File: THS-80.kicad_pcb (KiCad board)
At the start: 4 copper layers, 101.6 x 102.1 mm, 117 parts, among them J1 USB_B_Micro, J10 CT0, J2 RC80 Bus, J3 RC80 Expansion, J4 IDE, J5 JTAG, J6 PMOD, J7 PIO Header, J8 Port A, J9 Port A, SW1 Reset, SW2 SW_DIP_x06, SW3 User PB, U1 MAX40203AUK, U10 AP7381-33SA, U11 TXS0108EPW, U12 74HCT3G04, U2 DS1813R-5+T&R, U3 EPM7064STC100, U4 Z84C0010AEG, U5 IS62C5128BL-45TLI, U6 SST39SF040, U7 Z84C2010AEG, U8 Z84C4310AEG, U9 Z84C3010AEG, X1 CFPS-72 50mhz

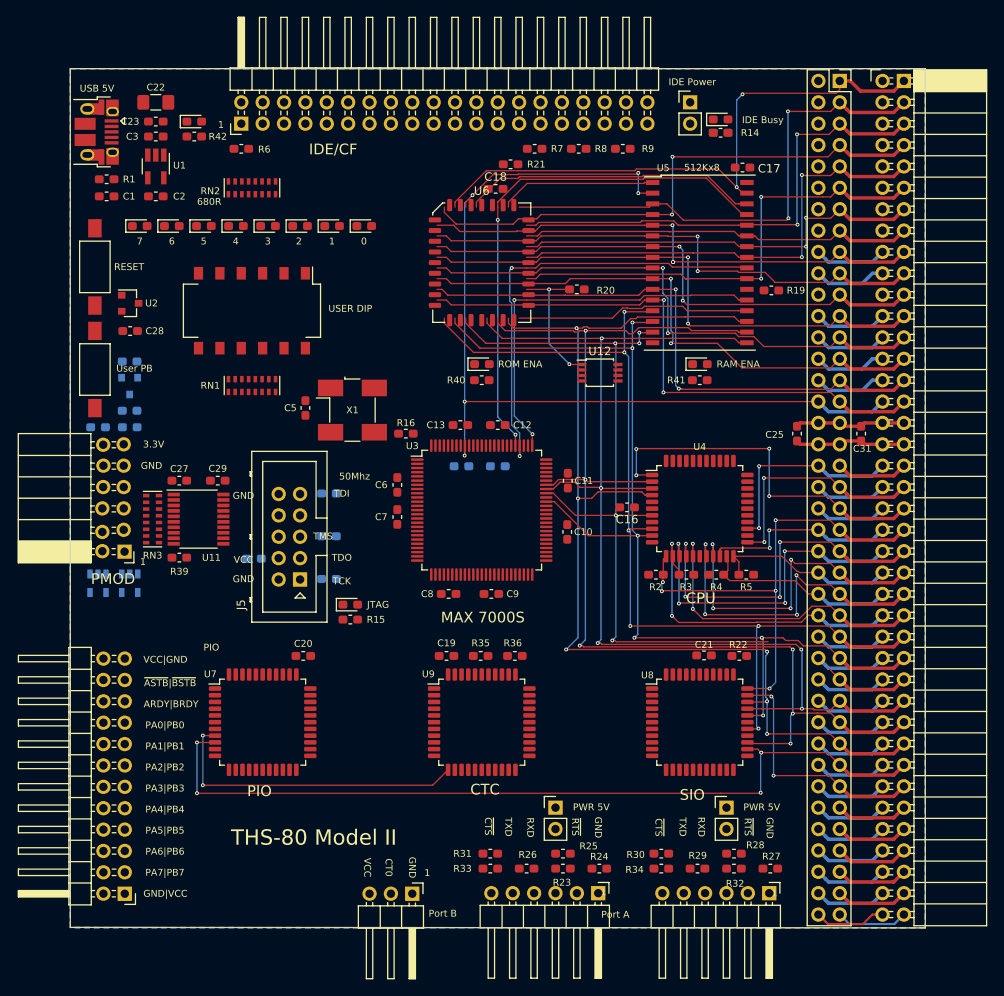
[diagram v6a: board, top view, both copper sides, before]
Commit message: layout changes, silkscreen fixes
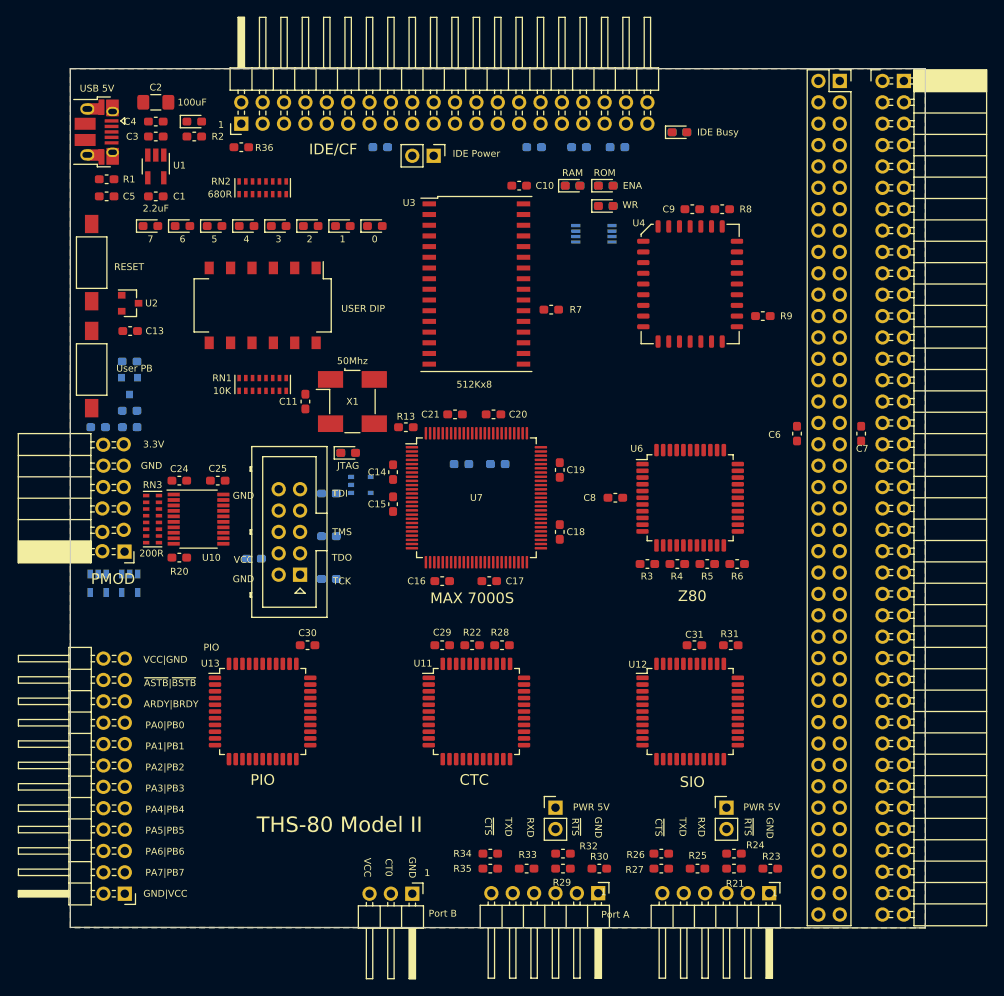
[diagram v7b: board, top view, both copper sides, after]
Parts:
- removed the D13 at (150.5, 66.7)
- removed the D14 at (176.4, 66.7)
- removed the R40 at (150.5, 68.6)
- removed R41: 360R, Resistor_SMD:R_0603_1608Metric_Pad1.05x0.95mm_HandSolder
- removed the U12 at (164.5, 67.7)
- removed the U6 at (150.5, 54.6)
- added D2: GRN, LED_SMD:LED_0603_1608Metric_Pad1.05x0.95mm_HandSolder, F.Cu at (165.2, 45.5)
- added D3: GRN, LED_SMD:LED_0603_1608Metric_Pad1.05x0.95mm_HandSolder, F.Cu at (161.3, 45.5)
- added D4: RED, LED_SMD:LED_0603_1608Metric_Pad1.05x0.95mm_HandSolder, F.Cu at (165.2, 47.9)
- added R10: 1K, Resistor_SMD:R_0603_1608Metric_Pad1.05x0.95mm_HandSolder, B.Cu at (165.2, 45.5)
- added R11: 1K, Resistor_SMD:R_0603_1608Metric_Pad1.05x0.95mm_HandSolder, B.Cu at (161.3, 45.5)
- added R12: 360R, Resistor_SMD:R_0603_1608Metric_Pad1.05x0.95mm_HandSolder, B.Cu at (165.2, 47.9)
- added U3: IS62C5128BL-45TLI, Package_SO:TSOP-II-32_21.0x10.2mm_P1.27mm, F.Cu at (149.9, 57.1)
- added U4: SST39SF040, Package_LCC:PLCC-32_11.4x14.0mm_P1.27mm, F.Cu at (175.3, 57.1)
- added U8: 74LVC1G04, Package_SO:TSOP-5_1.65x3.05mm_P0.95mm, B.Cu at (136.1, 81.0)
- R19: renamed from R15; moved to B.Cu
- R37: renamed from R7; moved to B.Cu
- R38: renamed from R8; moved to B.Cu
- R39: renamed from R9; moved to B.Cu
- R40: renamed from R14; moved to B.Cu
- U5: value IS62C5128BL-45TLI -> 74LVC2G02; footprint Package_SO:TSOP-II-32_21.0x10.2mm_P1.27mm -> Package_SO:TSSOP-8_3x3mm_P0.65mm; moved to B.Cu
- moved C28 40.5 mm to (138.4, 40.9), turned to 180 degrees
- moved JP3 31.1 mm to (144.8, 41.9), turned to 270 degrees
- moved R7 26.3 mm to (158.8, 60.2)
- moved R8 25.7 mm to (179.1, 48.3)
- moved R9 22.3 mm to (183.9, 61.0)
- moved R19 19.8 mm to (134.6, 77.2)
- moved D13 18.0 mm to (134.6, 77.2)
- moved U5 13.0 mm to (163.8, 51.2), turned to 180 degrees
- moved C9 7.76 mm to (175.5, 48.3)
- moved D16 5.12 mm to (174.0, 39.1)
- moved R40 4.89 mm to (174.0, 39.1)
- moved C10 2.82 mm to (154.9, 45.5), turned to 180 degrees
- moved R28 1.98 mm to (152.9, 100.1)
- moved C8 1.81 mm to (166.4, 82.5)
- moved U6 1.72 mm to (175.3, 82.5)
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- renumbered C2 to C1, C18 to C10, C5 to C11, C30 to C12, C28 to C13, C6 to C14, C7 to C15, C8 to C16, C9 to C17, C10 to C18, C11 to C19, C22 to C2, C12 to C20, C13 to C21, C14 to C22, C15 to C23, C27 to C24, C29 to C25, C24 to C26, C26 to C27, C4 to C28, C19 to C29, C20 to C30, C21 to C31, C23 to C4, C1 to C5, C25 to C6, C31 to C7, C16 to C8, C17 to C9, D15 to D1, D9 to D10, D10 to D11, D11 to D12, D2 to D13, D3 to D14, D12 to D15, D1 to D16, D4 to D5, D5 to D6, D6 to D7, D7 to D8, D8 to D9, J7 to J10, J5 to J4, J6 to J5, J10 to J6, J9 to J7, J4 to J9, JP3 to JP1, JP1 to JP3, R16 to R13, R17 to R14, R18 to R15, R11 to R16, R12 to R17, R10 to R18, R42 to R2, R39 to R20, R32 to R21, R35 to R22, R27 to R23, R28 to R24, R29 to R25, R30 to R26, R34 to R27, R36 to R28, R23 to R29, R2 to R3, R24 to R30, R22 to R31, R25 to R32, R26 to R33, R31 to R34, R33 to R35, R6 to R36, R3 to R4, R4 to R5, R5 to R6, R19 to R7, R21 to R8, R20 to R9, U11 to U10, U9 to U11, U8 to U12, U7 to U13, U4 to U6, U3 to U7, U10 to U9
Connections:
- C1 pad 1: +5V -> VCC
- C10 pad 1: +5V -> VCC
- C11 pad 1: +5V -> VCC
- C12 pad 1: +5V -> VCC
- C14 pad 1: +5V -> VCC
- C15 pad 1: +5V -> VCC
- C16 pad 1: +5V -> VCC
- C17 pad 1: +5V -> VCC
- C18 pad 1: +5V -> VCC
- C19 pad 1: +5V -> VCC
- C20 pad 1: +5V -> VCC
- C21 pad 1: +5V -> VCC
- C22 pad 1: +5V -> VCC
- C25 pad 1: +5V -> VCC
- C28 pad 1: +5V -> VCC
- C29 pad 1: +5V -> VCC
- C30 pad 1: +5V -> VCC
- C31 pad 1: +5V -> VCC
- C6 pad 1: +5V -> VCC
- C7 pad 1: +5V -> VCC
- C8 pad 1: +5V -> VCC
- C9 pad 1: +5V -> VCC
- D1 pad 2: +5V -> VCC
- J10 pad 1: +5V -> VCC
- J10 pad 24: +5V -> VCC
- J2 pad 35: +5V -> VCC
- J2 pad 36: +5V -> VCC
- J3 pad 35: +5V -> VCC
- J3 pad 36: +5V -> VCC
- J4 pad 4: +5V -> VCC
- J6 pad 3: +5V -> VCC
- JP1 pad 1: +5V -> VCC
- JP2 pad 1: +5V -> VCC
- JP3 pad 2: +5V -> VCC
- R14 pad 2: +5V -> VCC
- R15 pad 2: +5V -> VCC
- R16 pad 1: +5V -> VCC
- R17 pad 1: +5V -> VCC
- R21 pad 1: +5V -> VCC
- R22 pad 1: +5V -> VCC
- R28 pad 1: +5V -> VCC
- R29 pad 1: +5V -> VCC
- R3 pad 1: +5V -> VCC
- R31 pad 1: +5V -> VCC
- R36 pad 1: +5V -> VCC
- R37 pad 1: +5V -> VCC
- R38 pad 1: +5V -> VCC
- R39 pad 1: +5V -> VCC
- R4 pad 1: +5V -> VCC
- R40 pad 1: +5V -> VCC
- R5 pad 1: +5V -> VCC
- R6 pad 1: +5V -> VCC
- R7 pad 1: +5V -> VCC
- R8 pad 1: +5V -> VCC
- R9 pad 1: +5V -> VCC
- RN1 pad 10: +5V -> VCC
- RN1 pad 11: +5V -> VCC
- RN1 pad 12: +5V -> VCC
- RN1 pad 13: +5V -> VCC
- RN1 pad 14: +5V -> VCC
- RN1 pad 15: +5V -> VCC
- RN1 pad 16: +5V -> VCC
- RN1 pad 9: +5V -> VCC
- RN2 pad 10: +5V -> VCC
- RN2 pad 11: +5V -> VCC
- RN2 pad 12: +5V -> VCC
- RN2 pad 13: +5V -> VCC
- RN2 pad 14: +5V -> VCC
- RN2 pad 15: +5V -> VCC
- RN2 pad 16: +5V -> VCC
- RN2 pad 9: +5V -> VCC
- U1 pad 5: +5V -> VCC
- U10 pad 19: +5V -> VCC
- U11 pad 43: +5V -> VCC
- U12 pad 37: +5V -> VCC
- U13 pad 34: +5V -> VCC
- U2 pad 2: +5V -> VCC
- U5 pad 1: /A17 -> /RAM_~CE
- U5 pad 2: /A16 -> /RAM_~CE
- U5 pad 3: /A14 -> Net-(D4-Pad2)
- U5 pad 4: /A12 -> GND
- U5 pad 5: /A7 -> /ROM_~CE
- U5 pad 6: /A6 -> /~WR
- U5 pad 7: /A5 -> Net-(D2-Pad1)
- U5 pad 8: /A4 -> VCC
- U6 pad 6: +5V -> VCC
- U7 pad 18: +5V -> VCC
- U7 pad 3: +5V -> VCC
- U7 pad 34: +5V -> VCC
- U7 pad 39: +5V -> VCC
- U7 pad 51: +5V -> VCC
- U7 pad 66: +5V -> VCC
- U7 pad 82: +5V -> VCC
- U7 pad 91: +5V -> VCC
- U9 pad 1: +5V -> VCC
- X1 pad 1: +5V -> VCC
- X1 pad 4: +5V -> VCC
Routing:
- net /D4: track 138.7 -> 0.00 mm, vias 6 -> 0
- net /D3: track 134.3 -> 0.00 mm, vias 5 -> 0
- net /D5: track 132.7 -> 0.00 mm, vias 6 -> 0
- net /D6: track 128.3 -> 0.00 mm, vias 4 -> 0
- net /D1: track 122.7 -> 0.00 mm, vias 6 -> 0
- net /D0: track 115.1 -> 0.00 mm, vias 6 -> 0
- net /D7: track 113.0 -> 0.00 mm, vias 6 -> 0
- net /A16: track 109.9 -> 0.00 mm, vias 5 -> 0
- net /D2: track 103.3 -> 0.00 mm, vias 5 -> 0
- net /~WR: track 101.6 -> 0.00 mm, vias 6 -> 0
- net /~RD: track 92.7 -> 0.00 mm, vias 6 -> 0
- net /A15: track 70.9 -> 0.00 mm, vias 2 -> 0
- net /A1: track 69.1 -> 0.00 mm, vias 2 -> 0
- net /A0: track 68.5 -> 0.00 mm, vias 2 -> 0
- net /A2: track 66.5 -> 0.00 mm, vias 2 -> 0
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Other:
- board text added: "ENA"
- board text added: "RAM"
- board text added: "ROM"
- board text added: "WR"
- board text added: "Z80"
- board text removed: "CPU"
- board text removed: "RAM ENA"
- board text removed: "ROM ENA"

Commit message: more layout changes
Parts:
- moved D2 5.98 mm to (164.0, 51.3)
- moved R10 5.98 mm to (164.0, 51.3)
- moved D3 5.98 mm to (160.0, 51.3)
- moved R11 5.98 mm to (160.0, 51.3)
- moved D4 5.48 mm to (164.0, 53.2)
- moved R12 5.48 mm to (164.0, 53.2)
- moved U5 5.48 mm to (162.6, 56.5)
- moved C10 0.25 mm to (154.9, 45.2)
- moved C9 0.25 mm to (175.5, 48.0)
- moved R8 0.25 mm to (179.1, 48.0)
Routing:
- net /A15: track 0.00 -> 0.95 mm
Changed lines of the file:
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@@
     (thickness 1.6)
     (drawings 76)
-    (tracks 0)
+    (tracks 1)
     (zones 0)
     (modules 120)
@@
     (1 In1.Cu signal hide)
     (2 In2.Cu power hide)
-    (31 B.Cu signal)
+    (31 B.Cu signal hide)
     (34 B.Paste user hide)
     (35 F.Paste user hide)
@@
     (add_net "Net-(D8-Pad2)")
     (add_net "Net-(D9-Pad2)")
-    (add_net "Net-(J1-Pad2)")
-    (add_net "Net-(J1-Pad3)")
-    (add_net "Net-(J2-Pad10)")
-    (add_net "Net-(J2-Pad12)")
-    (add_net "Net-(J2-Pad14)")
-    (add_net "Net-(J2-Pad16)")
-    (add_net "Net-(J2-Pad2)")
-    (add_net "Net-(J2-Pad4)")
-    (add_net "Net-(J2-Pad6)")
-    (add_net "Net-(J2-Pad8)")
-    (add_net "Net-(J3-Pad10)")
-    (add_net "Net-(J3-Pad12)")
-    (add_net "Net-(J3-Pad14)")
-    (add_net "Net-(J3-Pad16)")
-    (add_net "Net-(J3-Pad2)")
-    (add_net "Net-(J3-Pad4)")
-    (add_net "Net-(J3-Pad6)")
-    (add_net "Net-(J3-Pad8)")
-    (add_net "Net-(J4-Pad6)")
-    (add_net "Net-(J4-Pad7)")
-    (add_net "Net-(J4-Pad8)")
     (add_net "Net-(J7-Pad3)")
     (add_net "Net-(J8-Pad3)")
-    (add_net "Net-(J9-Pad10)")
-    (add_net "Net-(J9-Pad12)")
-    (add_net "Net-(J9-Pad14)")
-    (add_net "Net-(J9-Pad16)")
-    (add_net "Net-(J9-Pad18)")
     (add_net "Net-(J9-Pad20)")
-    (add_net "Net-(J9-Pad21)")
-    (add_net "Net-(J9-Pad27)")
-    (add_net "Net-(J9-Pad28)")
     (add_net "Net-(J9-Pad29)")
-    (add_net "Net-(J9-Pad31)")
-    (add_net "Net-(J9-Pad32)")
     (add_net "Net-(J9-Pad34)")
     (add_net "Net-(J9-Pad38)")
-    (add_net "Net-(J9-Pad4)")
-    (add_net "Net-(J9-Pad6)")
-    (add_net "Net-(J9-Pad8)")
     (add_net "Net-(R13-Pad1)")
     (add_net "Net-(R14-Pad1)")
-    (add_net "Net-(RN1-Pad4)")
-    (add_net "Net-(RN1-Pad5)")
     (add_net "Net-(RN3-Pad10)")
     (add_net "Net-(RN3-Pad11)")
@@
     (add_net "Net-(RN3-Pad16)")
     (add_net "Net-(RN3-Pad9)")
-    (add_net "Net-(U1-Pad4)")
-    (add_net "Net-(U11-Pad11)")
-    (add_net "Net-(U11-Pad15)")
-    (add_net "Net-(U11-Pad16)")
-    (add_net "Net-(U11-Pad17)")
-    (add_net "Net-(U11-Pad19)")
-    (add_net "Net-(U11-Pad20)")
-    (add_net "Net-(U11-Pad24)")
-    (add_net "Net-(U11-Pad26)")
-    (add_net "Net-(U11-Pad28)")
-    (add_net "Net-(U11-Pad30)")
-    (add_net "Net-(U11-Pad34)")
-    (add_net "Net-(U11-Pad38)")
-    (add_net "Net-(U11-Pad39)")
-    (add_net "Net-(U11-Pad42)")
-    (add_net "Net-(U11-Pad44)")
-    (add_net "Net-(U11-Pad5)")
-    (add_net "Net-(U11-Pad6)")
-    (add_net "Net-(U11-Pad7)")
-    (add_net "Net-(U12-Pad1)")
-    (add_net "Net-(U12-Pad10)")
-    (add_net "Net-(U12-Pad15)")
-    (add_net "Net-(U12-Pad16)")
-    (add_net "Net-(U12-Pad17)")
-    (add_net "Net-(U12-Pad28)")
-    (add_net "Net-(U12-Pad38)")
-    (add_net "Net-(U12-Pad39)")
-    (add_net "Net-(U12-Pad40)")
-    (add_net "Net-(U13-Pad2)")
-    (add_net "Net-(U13-Pad28)")
-    (add_net "Net-(U13-Pad39)")
-    (add_net "Net-(U6-Pad11)")
-    (add_net "Net-(U6-Pad17)")
-    (add_net "Net-(U6-Pad33)")
-    (add_net "Net-(U6-Pad39)")
-    (add_net "Net-(U7-Pad1)")
-    (add_net "Net-(U7-Pad2)")
-    (add_net "Net-(U7-Pad22)")
-    (add_net "Net-(U7-Pad24)")
-    (add_net "Net-(U7-Pad27)")
-    (add_net "Net-(U7-Pad28)")
-    (add_net "Net-(U7-Pad37)")
-    (add_net "Net-(U7-Pad49)")
-    (add_net "Net-(U7-Pad5)")
-    (add_net "Net-(U7-Pad50)")
-    (add_net "Net-(U7-Pad53)")
-    (add_net "Net-(U7-Pad55)")
-    (add_net "Net-(U7-Pad7)")
-    (add_net "Net-(U7-Pad70)")
-    (add_net "Net-(U7-Pad72)")
-    (add_net "Net-(U7-Pad77)")
-    (add_net "Net-(U7-Pad78)")
     (add_net VCC)
   )
@@
   )
   (module Package_SO:TSSOP-8_3x3mm_P0.65mm (layer B.Cu)
-    (at 163.83 51.181 180)
+    (at 162.56 56.515 180)
     (descr "TSSOP8: plastic thin shrink small outline package; 8 leads; body width 3 mm; (see NXP SSOP-TSSOP-VSO-REFLOW.pdf and sot505-1_po.pdf)")
     (tags "SSOP 0.65")
@@
   )
   (module Resistor_SMD:R_0603_1608Metric_Pad1.05x0.95mm_HandSolder (layer B.Cu)
-    (at 165.227 47.879)
+    (at 163.957 53.213)
     (descr "Resistor SMD 0603 (1608 Metric), square (rectangular) end terminal, IPC_7351 nominal with elongated pad for handsoldering. (Body size source: http://www.tortai-tech.com/upload/download/2011102023233369053.pdf), generated with kicad-footprint-generator")
     (tags "resistor handsolder")
@@
   )
   (module Resistor_SMD:R_0603_1608Metric_Pad1.05x0.95mm_HandSolder (layer B.Cu)
-    (at 161.29 45.466 180)
+    (at 160.02 51.308 180)
     (descr "Resistor SMD 0603 (1608 Metric), square (rectangular) end terminal, IPC_7351 nominal with elongated pad for handsoldering. (Body size source: http://www.tortai-tech.com/upload/download/2011102023233369053.pdf), generated with kicad-footprint-generator")
     (tags "resistor handsolder")
@@
   )
   (module Resistor_SMD:R_0603_1608Metric_Pad1.05x0.95mm_HandSolder (layer B.Cu)
-    (at 165.227 45.466 180)
+    (at 163.957 51.308 180)
     (descr "Resistor SMD 0603 (1608 Metric), square (rectangular) end terminal, IPC_7351 nominal with elongated pad for handsoldering. (Body size source: http://www.tortai-tech.com/upload/download/2011102023233369053.pdf), generated with kicad-footprint-generator")
     (tags "resistor handsolder")
@@
   )
   (module LED_SMD:LED_0603_1608Metric_Pad1.05x0.95mm_HandSolder (layer F.Cu)
-    (at 165.227 47.879)
+    (at 163.957 53.213)
     (descr "LED SMD 0603 (1608 Metric), square (rectangular) end terminal, IPC_7351 nominal, (Body size source: http://www.tortai-tech.com/upload/download/2011102023233369053.pdf), generated with kicad-footprint-generator")
     (tags "LED handsolder")
@@
   )
   (module LED_SMD:LED_0603_1608Metric_Pad1.05x0.95mm_HandSolder (layer F.Cu)
-    (at 161.29 45.466)
+    (at 160.02 51.308)
     (descr "LED SMD 0603 (1608 Metric), square (rectangular) end terminal, IPC_7351 nominal, (Body size source: http://www.tortai-tech.com/upload/download/2011102023233369053.pdf), generated with kicad-footprint-generator")
     (tags "LED handsolder")
@@
   )
   (module LED_SMD:LED_0603_1608Metric_Pad1.05x0.95mm_HandSolder (layer F.Cu)
-    (at 165.227 45.466)
+    (at 163.957 51.308)
     (descr "LED SMD 0603 (1608 Metric), square (rectangular) end terminal, IPC_7351 nominal, (Body size source: http://www.tortai-tech.com/upload/download/2011102023233369053.pdf), generated with kicad-footprint-generator")
     (tags "LED handsolder")
@@
   )
   (module Capacitor_SMD:C_0603_1608Metric_Pad1.05x0.95mm_HandSolder (layer F.Cu)
-    (at 154.94 45.466 180)
+    (at 154.94 45.212 180)
     (descr "Capacitor SMD 0603 (1608 Metric), square (rectangular) end terminal, IPC_7351 nominal with elongated pad for handsoldering. (Body size source: http://www.tortai-tech.com/upload/download/2011102023233369053.pdf), generated with kicad-footprint-generator")
     (tags "capacitor handsolder")
@@
   )
   (module Capacitor_SMD:C_0603_1608Metric_Pad1.05x0.95mm_HandSolder (layer F.Cu)
-    (at 175.514 48.26 180)
+    (at 175.514 48.006 180)
     (descr "Capacitor SMD 0603 (1608 Metric), square (rectangular) end terminal, IPC_7351 nominal with elongated pad for handsoldering. (Body size source: http://www.tortai-tech.com/upload/download/2011102023233369053.pdf), generated with kicad-footprint-generator")
     (tags "capacitor handsolder")
@@
   )
   (module Resistor_SMD:R_0603_1608Metric_Pad1.05x0.95mm_HandSolder (layer F.Cu)
-    (at 179.07 48.26 180)
+    (at 179.07 48.006 180)
     (descr "Resistor SMD 0603 (1608 Metric), square (rectangular) end terminal, IPC_7351 nominal with elongated pad for handsoldering. (Body size source: http://www.tortai-tech.com/upload/download/2011102023233369053.pdf), generated with kicad-footprint-generator")
     (tags "resistor handsolder")
@@
     )
   )
-  (gr_text WR (at 168.148 47.752) (layer F.SilkS)
+  (gr_text WR (at 166.878 53.086) (layer F.SilkS)
     (effects (font (size 0.8128 0.8128) (thickness 0.1524)))
   )
-  (gr_text ENA (at 168.402 45.466) (layer F.SilkS)
+  (gr_text ENA (at 167.132 51.308) (layer F.SilkS)
     (effects (font (size 0.8128 0.8128) (thickness 0.1524)))
   )
@@
     (effects (font (size 0.8128 0.8128) (thickness 0.1524)))
   )
-  (gr_text RAM (at 161.29 43.942) (layer F.SilkS)
+  (gr_text RAM (at 160.02 49.784) (layer F.SilkS)
     (effects (font (size 0.8128 0.8128) (thickness 0.1524)))
   )
@@
     (effects (font (size 0.8128 0.8128) (thickness 0.1524)))
   )
-  (gr_text ROM (at 165.1 43.942) (layer F.SilkS)
+  (gr_text ROM (at 163.83 49.784) (layer F.SilkS)
     (effects (font (size 0.8128 0.8128) (thickness 0.1524)))
   )
@@
   (gr_line (start 203.2 31.5595) (end 203.2 133.6675) (layer Edge.Cuts) (width 0.1016))
   (gr_line (start 101.6 133.604) (end 101.6 31.5595) (layer Edge.Cuts) (width 0.1))
+  (segment (start 156.4124 48.895) (end 155.46 48.895) (width 0.1524) (layer F.Cu) (net 5))
   (zone (net 1) (net_name GND) (layer In1.Cu) (hatch edge 0.508)
     (connect_pads thru_hole_only (clearance 0.1524))
